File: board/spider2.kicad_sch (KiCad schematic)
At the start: 110 parts, among them J1 NRJ6HH, J10 PJ-320A, J11 PJ359, J12 PJ359, J13 PJ359, J14 PJ359, J15 PJ359, J16 PJ359, J17 A, J19 PJ359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

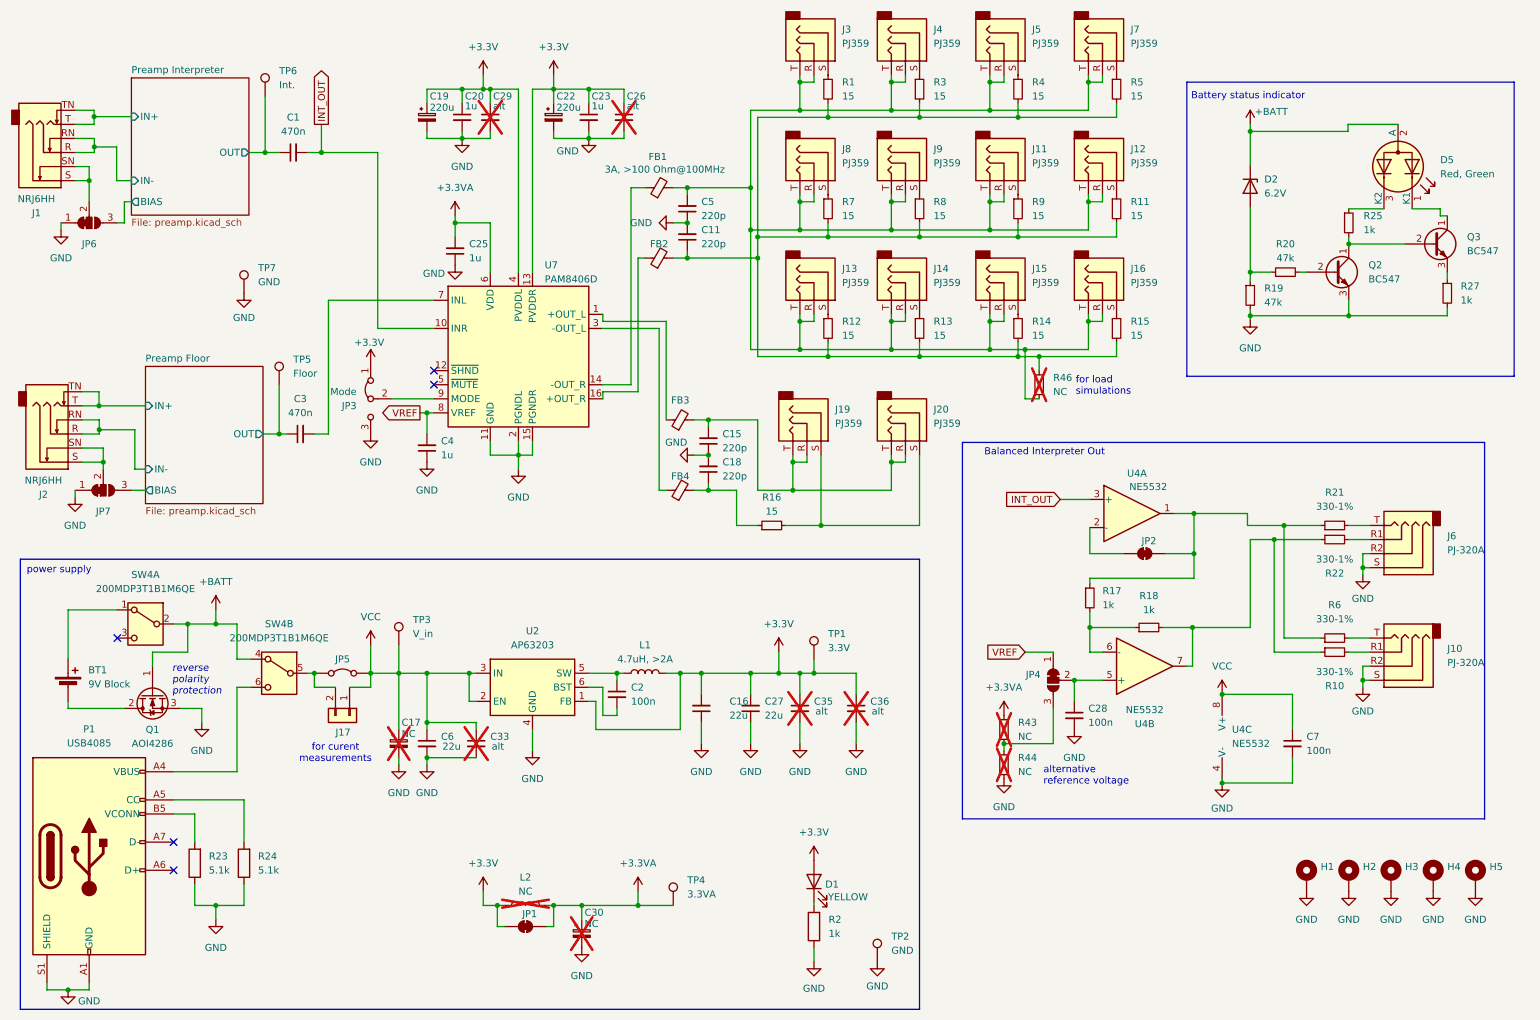
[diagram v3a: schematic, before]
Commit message: clean up not required components
jumpers, some dnp components, etc.
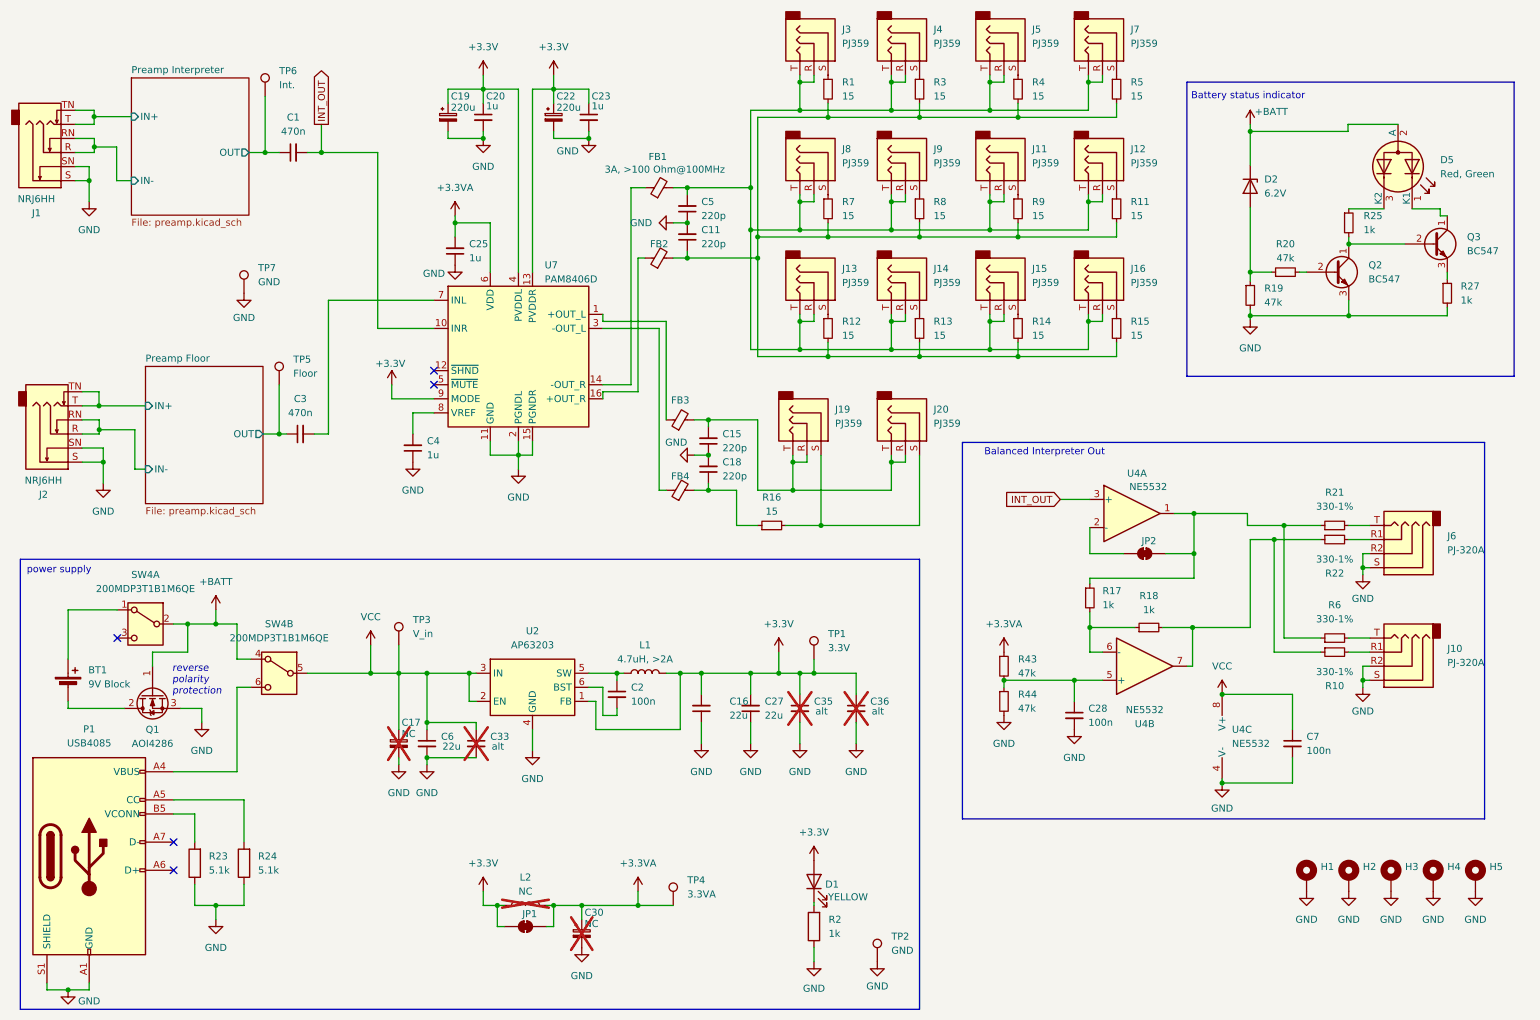
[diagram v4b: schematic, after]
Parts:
- removed C26, C29: alt, Capacitor_SMD:C_0805_2012Metric_Pad1.18x1.45mm_HandSolder, symbol Device:C_Small
- removed J17: A, Connector_PinHeader_2.54mm:PinHeader_1x02_P2.54mm_Vertical, symbol Connector_Generic:Conn_01x02
- removed JP3: Mode, Jumper:SolderJumper-3_P1.3mm_Bridged12_RoundedPad1.0x1.5mm, symbol Jumper:Jumper_3_Bridged12
- removed JP4, JP6, JP7: SolderJumper_3_Bridged12, Jumper:SolderJumper-3_P1.3mm_Bridged12_RoundedPad1.0x1.5mm, symbol Jumper:SolderJumper_3_Bridged12
- removed JP5: Jumper_2_Bridged, Jumper:SolderJumper-2_P1.3mm_Bridged_RoundedPad1.0x1.5mm, symbol Jumper:Jumper_2_Bridged
- removed R46: NC, Resistor_THT:R_Axial_Power_L25.0mm_W9.0mm_P7.62mm_Vertical, symbol Device:R_Small
- R43, R44: value NC -> 47k; now fitted
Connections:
- net +3.3V: now also U7.9 (MODE)
- net GND: now also J1.S, J1.SN, J2.S, J2.SN
- net VCC: now also SW4.5 (B)
- net at C28.1, U4.5 (+): now also R43.2, R44.1
- net VREF: no longer names the net of C4.2, U7.8 (VREF)
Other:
- sheet Preamp Floor ports: added none; removed BIAS
- sheet Preamp Interpreter ports: added none; removed BIAS
- note removed: "alternative reference voltage"
- note removed: "for curent measurements"
- note removed: "for load simulations"
- moved on the sheet: C19, C20, C4

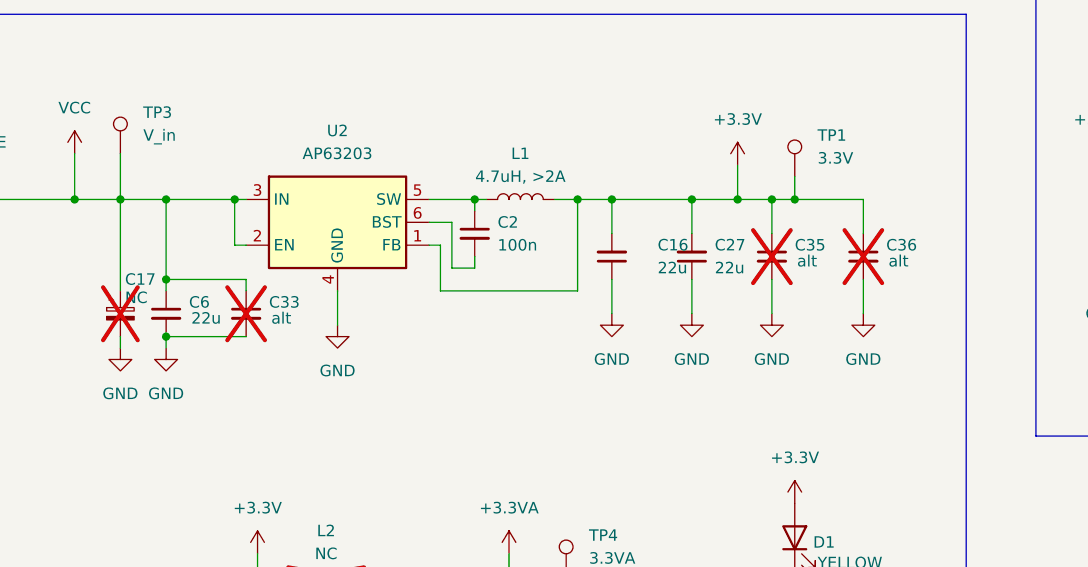
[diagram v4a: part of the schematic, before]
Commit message: bypass capacitor footprints smaller and closer
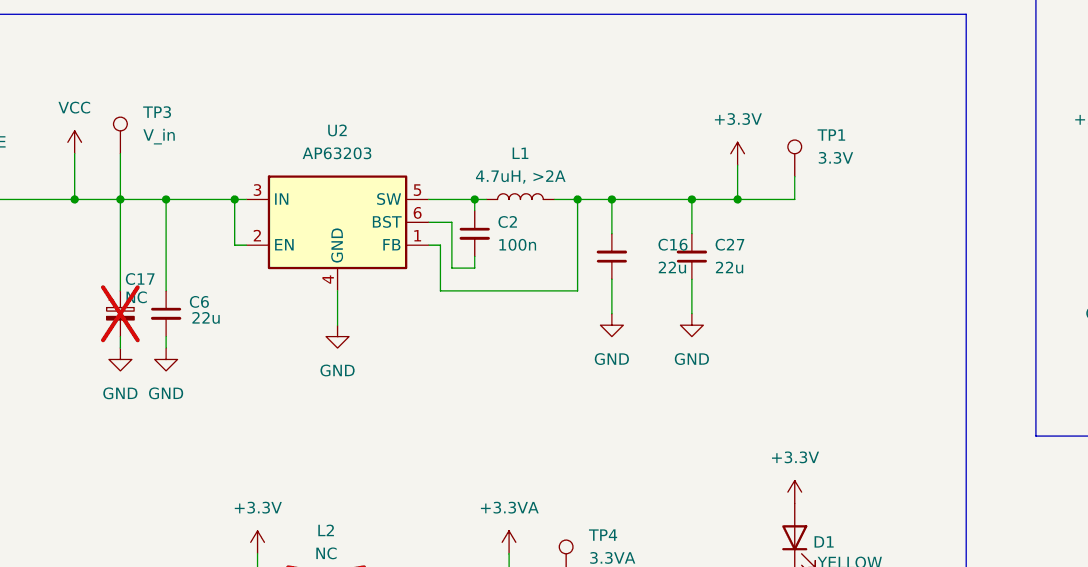
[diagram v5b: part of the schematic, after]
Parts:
- removed C33, C35, C36: alt, Capacitor_SMD:C_1210_3225Metric_Pad1.33x2.70mm_HandSolder, symbol Device:C_Small
- C11, C15, C16, C18, C20, C23, C25, C27, C4, C5, C6: footprint Capacitor_THT:C_Disc_D5.1mm_W3.2mm_P5.00mm -> Capacitor_THT:C_Disc_D4.3mm_W1.9mm_P5.00mm

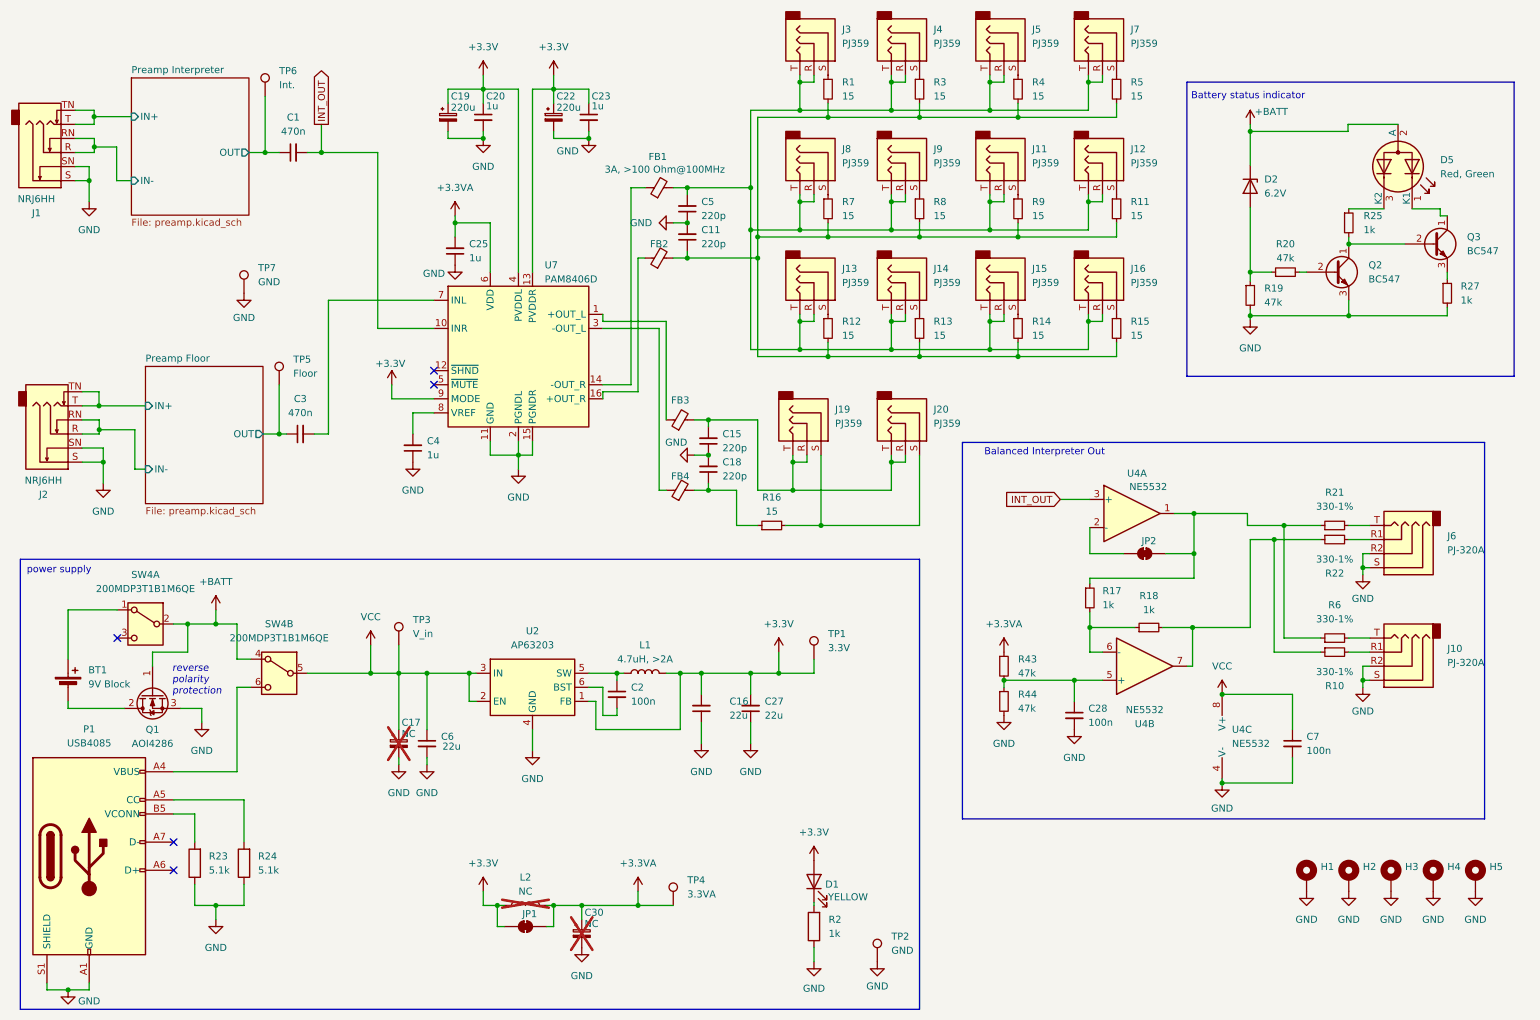
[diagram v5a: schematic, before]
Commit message: multiple changes
- correct transistor footprints
- swap led green/red
- PAM input resistor
- poti adjustments
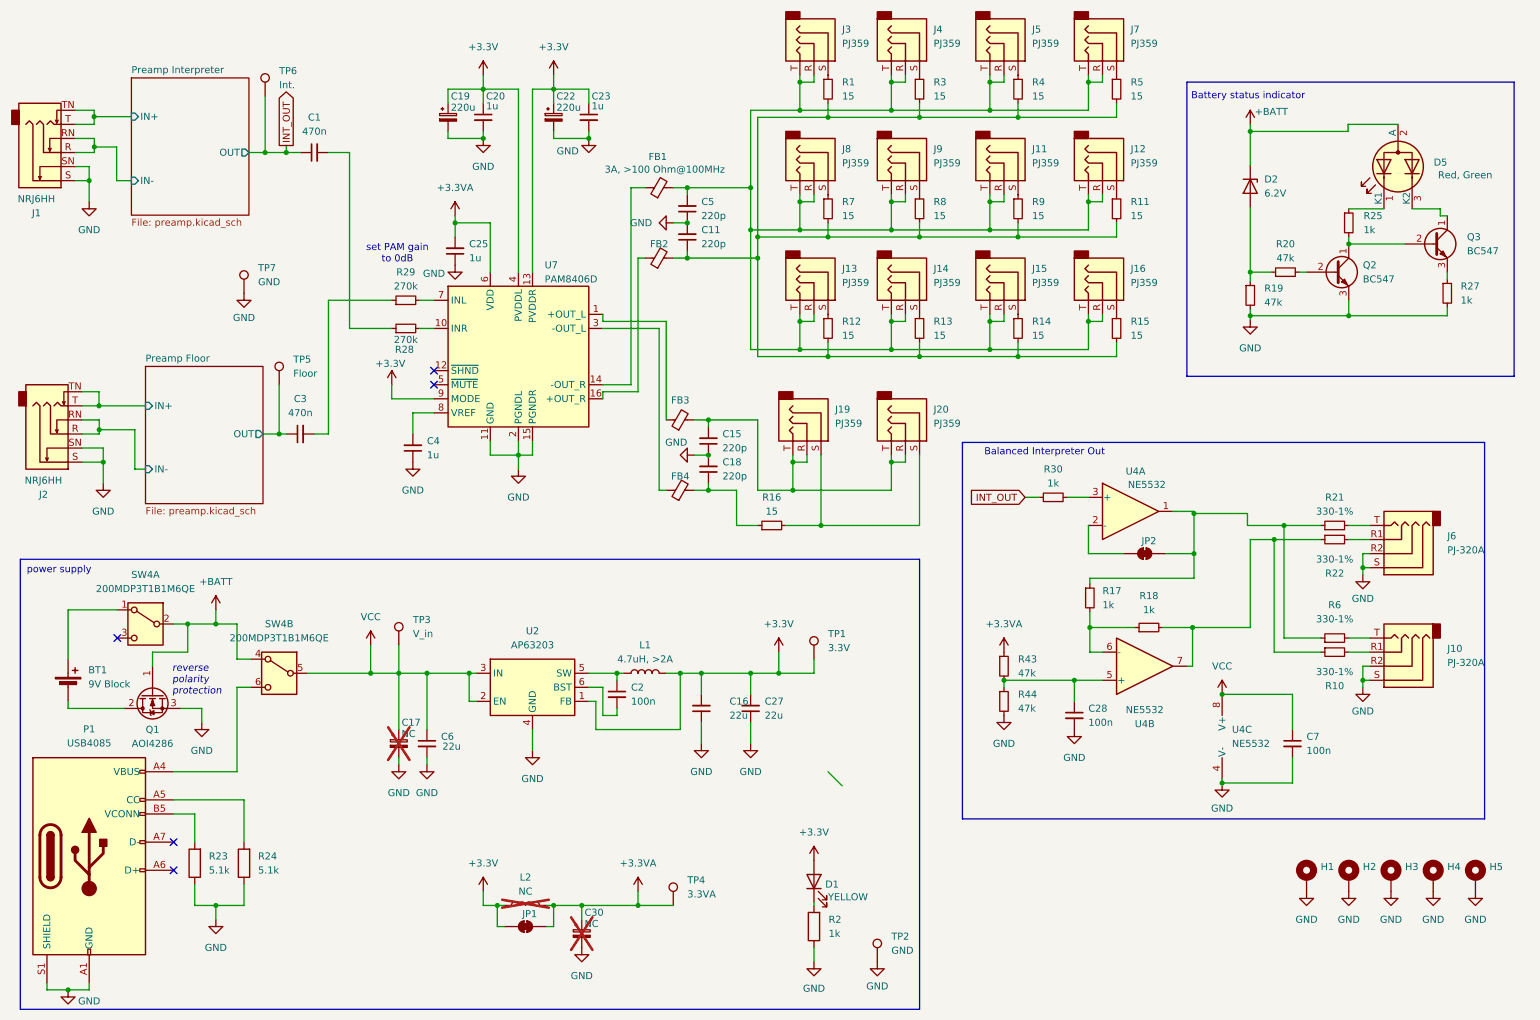
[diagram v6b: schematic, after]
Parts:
- added R28, R29: 270k, Resistor_THT:R_Axial_DIN0207_L6.3mm_D2.5mm_P10.16mm_Horizontal, symbol Device:R_Small
- added R30: 1k, Resistor_THT:R_Axial_DIN0207_L6.3mm_D2.5mm_P10.16mm_Horizontal, symbol Device:R_Small
- Q2, Q3: footprint Package_TO_SOT_THT:TO-92_Inline -> Package_TO_SOT_THT:TO-92_Inline_Wide
- TP5, TP6: footprint TestPoint:TestPoint_THTPad_1.5x1.5mm_Drill0.7mm -> TestPoint:TestPoint_THTPad_3.0x3.0mm_Drill1.5mm
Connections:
- net Preamp Interpreter/OUT is gone; now on net INT_OUT: C1.1, TP6.1
- net INT_OUT: now also R30.1; no longer C1.2, U4.3 (+), U7.10 (INR)
- net at R25.1: now also D5.1 (K1); no longer D5.3 (K2)
- net at C3.2: now also R29.1; no longer U7.7 (INL)
- net at Q3.1 (C): now also D5.3 (K2); no longer D5.1 (K1)
- new net: R29.2, U7.7 (INL)
- new net: R30.2, U4.3 (+)
- new net: R28.2, U7.10 (INR)
- new net: C1.2, R28.1
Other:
- note added: "set PAM gain to 0dB"
- moved on the sheet: C1, D5
